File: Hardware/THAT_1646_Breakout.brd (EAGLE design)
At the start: 45.7 x 20.3 mm, 28 parts, among them IC1 THAT1646, J1 1x4, J2 SN, J3 CHASSIS, J4 TN, J5 RN, J6 OUTPUT

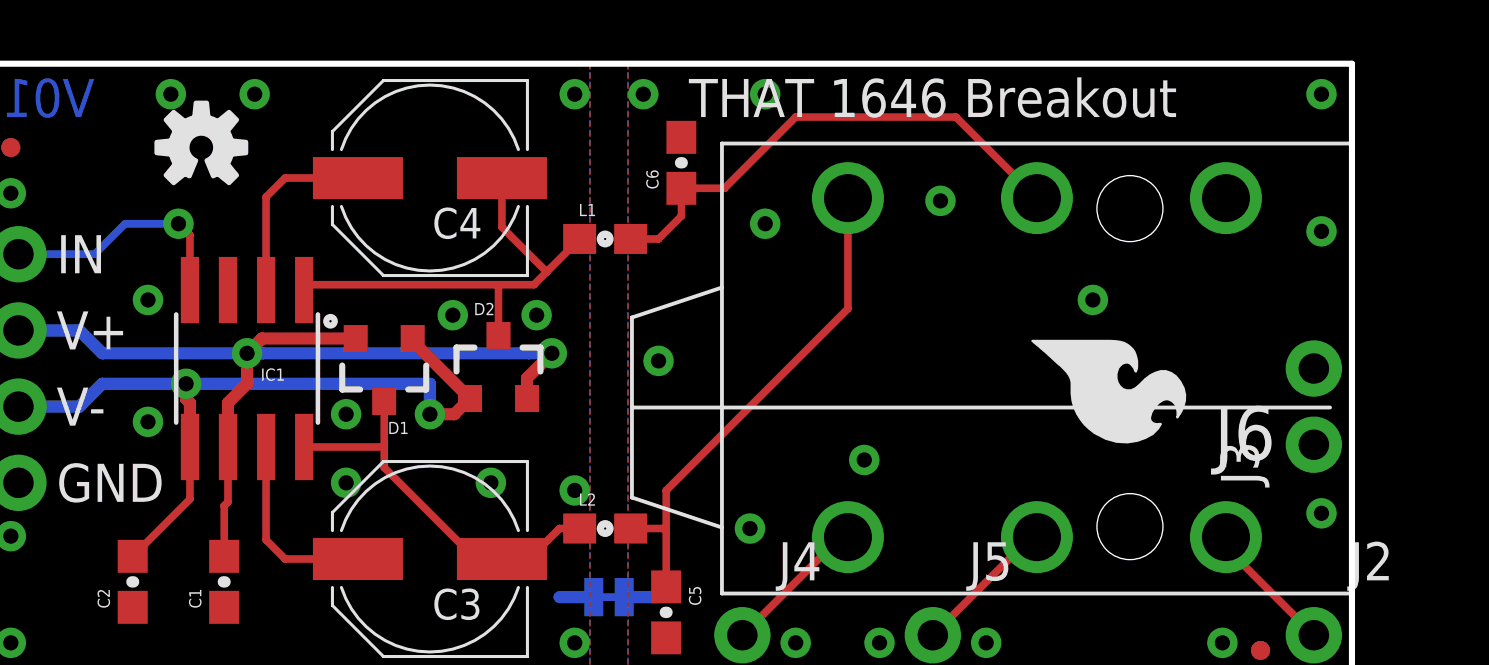
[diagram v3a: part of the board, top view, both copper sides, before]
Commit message: Addressing Kade's checklist issues.
-Via under "THAT" in top silk
-Nixing "Toed"
-90-deg trace on bottom made 45.
-Moved chassis connection out from under TRS.
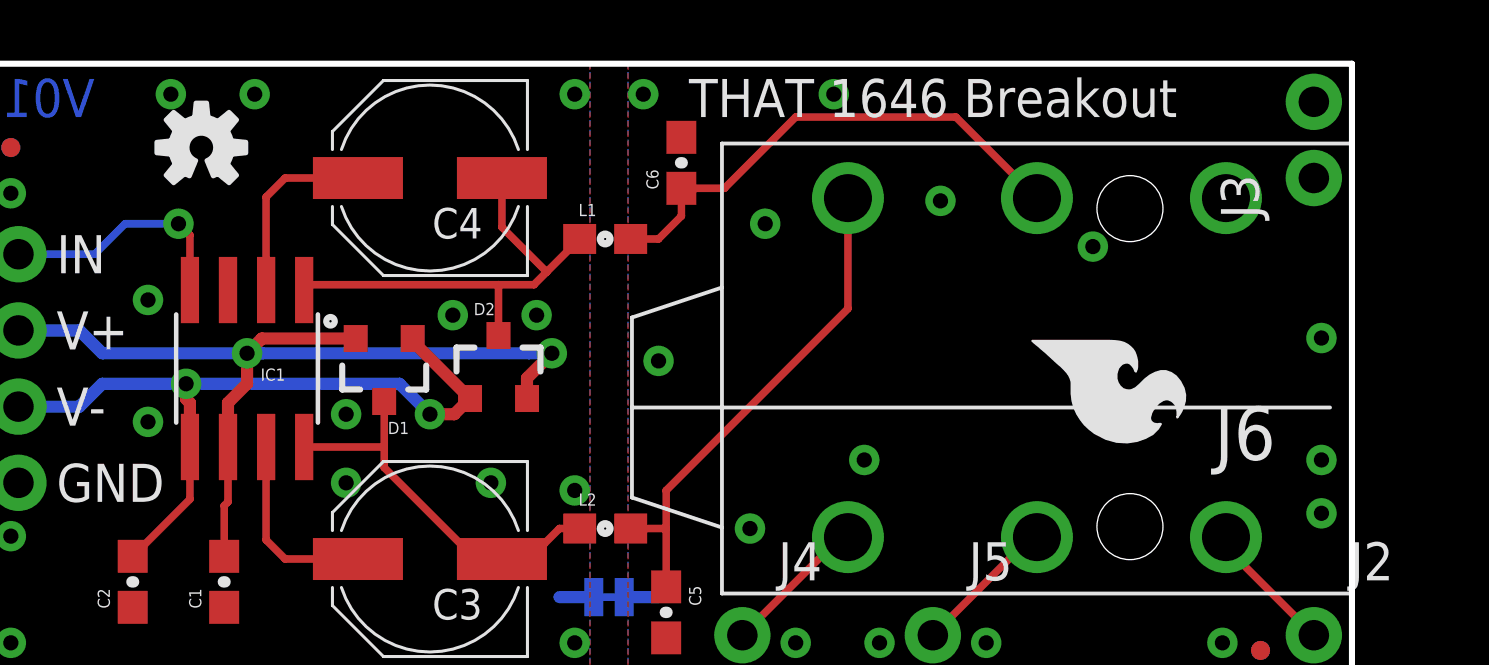
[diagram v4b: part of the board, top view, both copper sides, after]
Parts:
- moved J3 8.89 mm to (44.5, 16.5)
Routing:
- net VNEG: track 26.0 -> 25.4 mm
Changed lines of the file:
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@@
 <setting verticaltext="up"/>
 </settings>
-<grid distance="0.01" unitdist="inch" unit="inch" style="lines" multiple="1" display="yes" altdistance="0.005" altunitdist="inch" altunit="inch"/>
+<grid distance="0.05" unitdist="inch" unit="inch" style="lines" multiple="1" display="yes" altdistance="0.005" altunitdist="inch" altunit="inch"/>
 <layers>
 <layer number="1" name="Top" color="4" fill="1" visible="yes" active="yes"/>
@@
 <layer number="37" name="tTest" color="7" fill="1" visible="no" active="yes"/>
 <layer number="38" name="bTest" color="7" fill="1" visible="no" active="yes"/>
-<layer number="39" name="tKeepout" color="4" fill="11" visible="yes" active="yes"/>
-<layer number="40" name="bKeepout" color="1" fill="11" visible="yes" active="yes"/>
+<layer number="39" name="tKeepout" color="4" fill="11" visible="no" active="yes"/>
+<layer number="40" name="bKeepout" color="1" fill="11" visible="no" active="yes"/>
 <layer number="41" name="tRestrict" color="4" fill="10" visible="no" active="yes"/>
 <layer number="42" name="bRestrict" color="1" fill="10" visible="no" active="yes"/>
@@
 <layer number="45" name="Holes" color="7" fill="1" visible="yes" active="yes"/>
 <layer number="46" name="Milling" color="3" fill="1" visible="no" active="yes"/>
-<layer number="47" name="Measures" color="7" fill="1" visible="yes" active="yes"/>
+<layer number="47" name="Measures" color="7" fill="1" visible="no" active="yes"/>
 <layer number="48" name="Document" color="7" fill="1" visible="no" active="yes"/>
 <layer number="49" name="Reference" color="7" fill="1" visible="no" active="yes"/>
@@
 isolate chassis
 and circuit grounds</text>
-<text x="42.164" y="6.35" size="1.27" layer="22" font="vector" ratio="15" rot="MR90">Chassis</text>
+<text x="44.45" y="15.494" size="1.27" layer="22" font="vector" ratio="15" rot="MR90" align="center-right">Chassis</text>
 <dimension x1="0" y1="0" x2="0" y2="20.32" x3="-5.842" y3="10.16" textsize="1.778" textratio="15" layer="47" unit="inch"/>
 <dimension x1="0" y1="0" x2="45.72" y2="0" x3="22.86" y3="-5.842" textsize="1.778" textratio="15" layer="47" unit="inch"/>
@@
 <attribute name="PROD_ID" value="CONN-09696" x="1.27" y="6.35" size="1.778" layer="27" font="vector" ratio="15" rot="R90" display="off"/>
 </element>
-<element name="J3" library="SparkFun-Connectors" package="1X02_NO_SILK" value="CHASSIS" x="44.45" y="7.62" rot="R90"/>
+<element name="J3" library="SparkFun-Connectors" package="1X02_NO_SILK" value="CHASSIS" x="44.45" y="16.51" rot="R90"/>
 <element name="FD3" library="SparkFun-Aesthetics" package="MICRO-FIDUCIAL" value="FIDUCIALUFIDUCIAL" x="1.016" y="17.526"/>
 <element name="FD4" library="SparkFun-Aesthetics" package="MICRO-FIDUCIAL" value="FIDUCIALUFIDUCIAL" x="42.672" y="0.762"/>
@@
 <wire x1="3.302" y1="8.89" x2="4.064" y2="9.652" width="0.4064" layer="16"/>
 <wire x1="4.064" y1="9.652" x2="6.858" y2="9.652" width="0.4064" layer="16"/>
-<wire x1="6.858" y1="9.652" x2="14.986" y2="9.652" width="0.4064" layer="16"/>
+<wire x1="6.858" y1="9.652" x2="13.97" y2="9.652" width="0.4064" layer="16"/>
 <via x="14.986" y="8.636" extent="1-16" drill="0.508"/>
-<wire x1="14.986" y1="8.636" x2="14.986" y2="9.652" width="0.4064" layer="16"/>
+<wire x1="14.986" y1="8.636" x2="13.97" y2="9.652" width="0.4064" layer="16"/>
 <wire x1="14.412" y1="11.16" x2="14.412" y2="11.07" width="0.254" layer="1"/>
 <wire x1="14.412" y1="11.07" x2="16.322" y2="9.16" width="0.4064" layer="1"/>
@@
 <wire x1="21.463" y1="2.54" x2="22.606" y2="2.54" width="0.4064" layer="16"/>
 <via x="22.098" y="19.304" extent="1-16" drill="0.508"/>
-<via x="26.162" y="19.304" extent="1-16" drill="0.508"/>
-<via x="44.704" y="19.304" extent="1-16" drill="0.508"/>
-<via x="44.704" y="14.732" extent="1-16" drill="0.508"/>
-<via x="37.084" y="12.446" extent="1-16" drill="0.508"/>
+<via x="28.448" y="19.304" extent="1-16" drill="0.508"/>
+<via x="37.084" y="14.224" extent="1-16" drill="0.508"/>
+<via x="44.704" y="7.112" extent="1-16" drill="0.508"/>
+<via x="44.704" y="11.176" extent="1-16" drill="0.508"/>
 <via x="29.464" y="7.112" extent="1-16" drill="0.508"/>
 <via x="29.972" y="1.016" extent="1-16" drill="0.508"/>
